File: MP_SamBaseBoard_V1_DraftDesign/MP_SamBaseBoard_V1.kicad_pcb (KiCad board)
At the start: 4 copper layers, 175 x 130.2 mm, 268 parts, among them J1 MOTOR-A_CONN, J10 P1_CONN, J11 I2C_CONN, J12 I2C_CONN, J13 SAM_SWD, J14 WS2812_EXT, J15 PWR_JACK, J16 USB_B_Micro, J17 BATT_CONN, J2 MOTOR-B_CONN, J3 Adafruit_Feather_CONN, J4 uSD_Card, J5 Conn_01x02, J6 Conn_01x02, J7 SERVO_CONN, J8 P3_CONN, J9 P2_CONN, Q1 DMP3098L, SW1 RESET, SW2 3v3_PWR_SW, SW3 SW1, SW4 SW2, U1 ESP32-WROOM-32, U10 MPU-6050, U11 IRFHM9331PbF, U12 BD5291FVE-GTR, U13 SST25VF016B-50-4C-S2AF, U2 ATSAMD51J19A-A, U3 74LVC1G125, U4 TPS62135, U5 TPS62086, U6 MAX98357AETE, U7 DRV8833RTY, U8 HDC1080, U9 MCP73871-1CC, Y1 Crystal

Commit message: update
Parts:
- added C44: 0.1uF, Capacitor_SMD:C_0603_1608Metric, F.Cu at (222.5, 179.0)
- added G***: LOGO, GiraffeTech-Utility:MakerPlayground_logo_4x4mm, F.Cu at (199.2, 182.5)
- moved R26 52.7 mm to (207.5, 179.0), turned to 270 degrees
- moved C33 52.1 mm to (210.5, 179.0), turned to 270 degrees
- moved U12 50.8 mm to (212.8, 179.0), turned to 90 degrees
- moved R27 50.3 mm to (209.0, 179.0), turned to 90 degrees
- moved R28 47.5 mm to (216.5, 179.0), turned to 270 degrees
- moved R29 44.3 mm to (215.0, 179.0), turned to 90 degrees
- moved C19 42.3 mm to (212.8, 176.5), turned to 180 degrees
- moved MK1 38.1 mm to (220.2, 179.0)
- moved C32 37.0 mm to (218.0, 179.0), turned to 90 degrees
- moved C30 34.1 mm to (228.0, 176.5)
- moved C22 21.4 mm to (264.2, 175.5)
- moved U8 21.4 mm to (267.0, 175.5)
- moved C28 18.5 mm to (240.5, 178.2), turned to 0 degrees
- moved R22 11.6 mm to (240.5, 179.8), turned to 180 degrees
- moved C29 10.1 mm to (246.8, 173.0), turned to 180 degrees
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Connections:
- U6 pad 16: D1_TxD0 -> GND
- U6 pad 17: GND -> (no net)
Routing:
- net +3V3: track 383.1 -> 427.8 mm
- net I2C_SDA: track 60.7 -> 82.1 mm
- net I2C_SCL: track 61.3 -> 81.1 mm
- net Adf_A5: track 13.2 -> 20.2 mm
- net Adf_D6: track 29.1 -> 23.1 mm
- net Net-(C33-Pad2): track 0.00 -> 5.44 mm
- net Net-(R28-Pad1): track 0.00 -> 4.88 mm
- net Net-(R22-Pad2): track 0.00 -> 4.22 mm
- net Net-(C28-Pad1): track 0.00 -> 3.39 mm
- net Net-(J6-Pad2): track 9.20 -> 11.8 mm
- net GND: track 42.9 -> 45.3 mm, vias 142 -> 174
- net Net-(C32-Pad2): track 0.00 -> 1.72 mm
- net Net-(C32-Pad1): track 0.00 -> 1.52 mm
- net Net-(C30-Pad1): track 0.00 -> 1.15 mm
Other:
- board text added: "MIC"

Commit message: update1
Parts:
- moved REF** 23.8 mm to (220.2, 205.8)
- moved C22 21.8 mm to (242.8, 179.0), turned to 90 degrees
- moved U8 21.0 mm to (246.0, 175.5)
- moved C29 6.73 mm to (240.5, 175.5), turned to 0 degrees
- moved C30 3.58 mm to (231.5, 175.8)
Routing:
- net Adf_D4: track 53.4 -> 84.2 mm
- net I2C_SDA: track 82.1 -> 103.1 mm, vias 1 -> 2
- net I2C_SCL: track 81.1 -> 96.1 mm, vias 1 -> 2
- net +3V3: track 427.8 -> 435.9 mm, vias 9 -> 12
- net SWDIO: track 16.4 -> 12.9 mm
- net GND: track 45.3 -> 48.1 mm, vias 174 -> 178
- net Adf_D13: track 35.8 -> 38.2 mm
- net SPI_MISO: track 81.6 -> 83.7 mm
- net SPI_SCK: track 85.6 -> 87.5 mm
- net SPI_MOSI: track 72.8 -> 74.7 mm
- net Adf_A4: track 41.4 -> 42.8 mm
- net SWCLK: track 12.7 -> 13.7 mm, vias 2 -> 1
- net Net-(C30-Pad1): track 1.15 -> 1.90 mm
- net SWO: track 14.5 -> 13.8 mm
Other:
- board text added: "6V-15V"
- board text added: "OFF"
- board text added: "TEMP&HUMID"

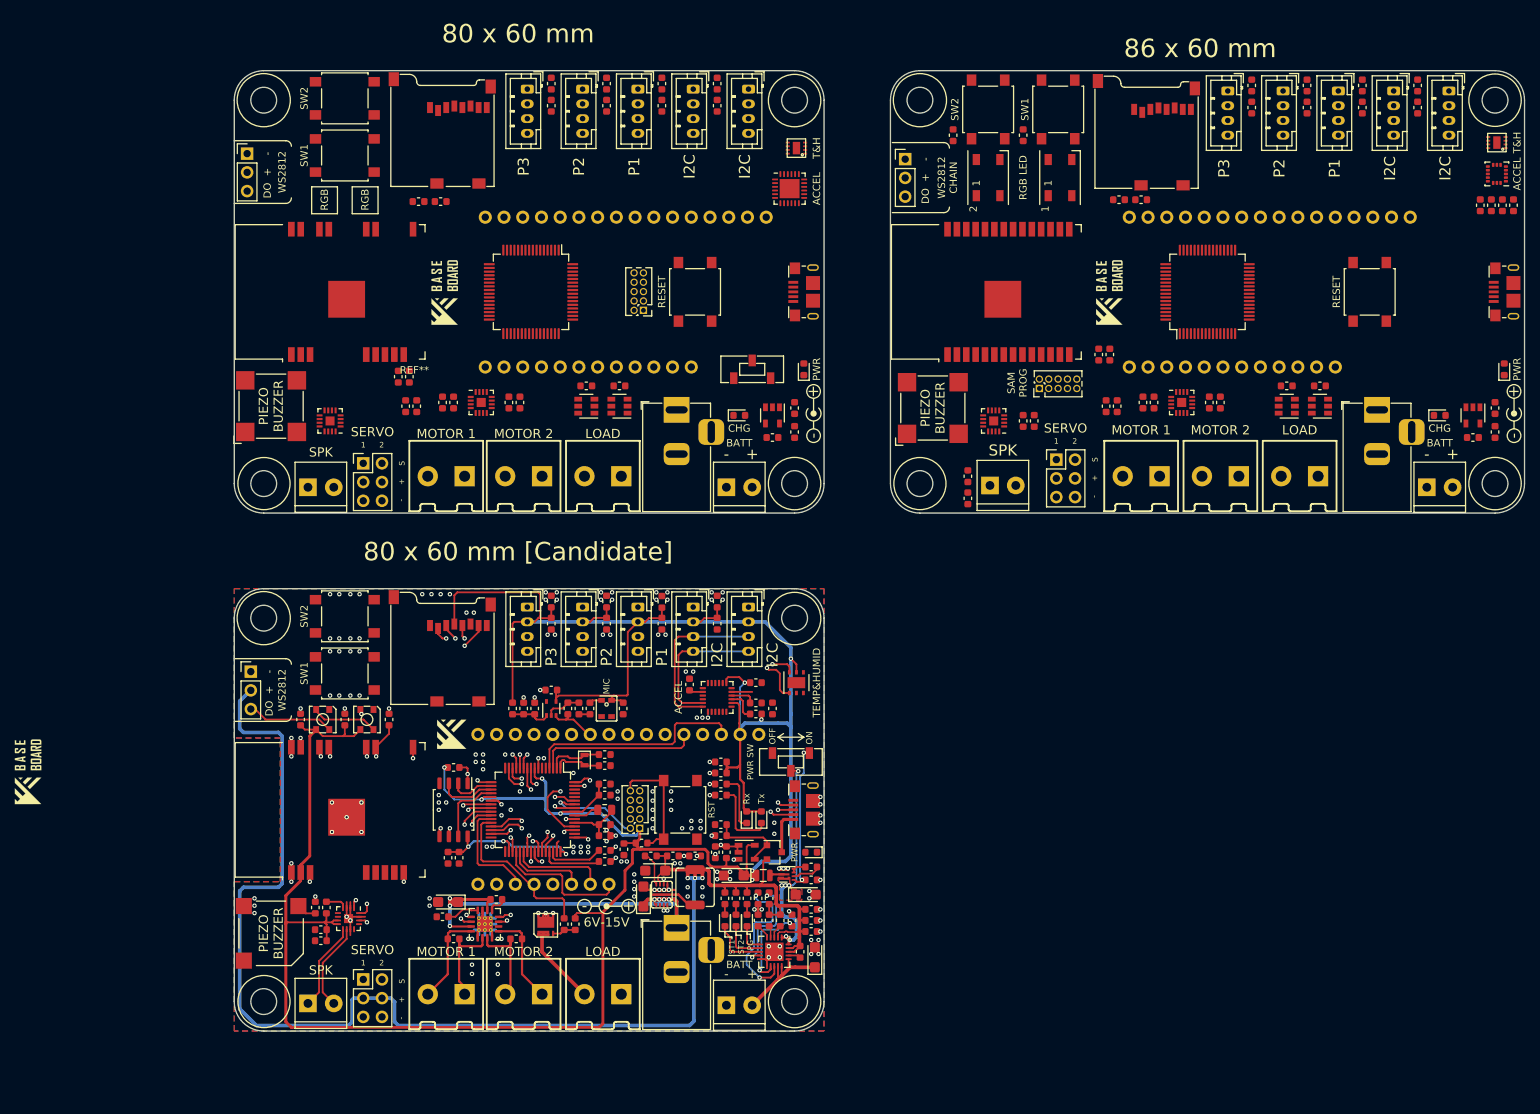
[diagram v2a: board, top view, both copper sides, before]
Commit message: Footprint replacement pending
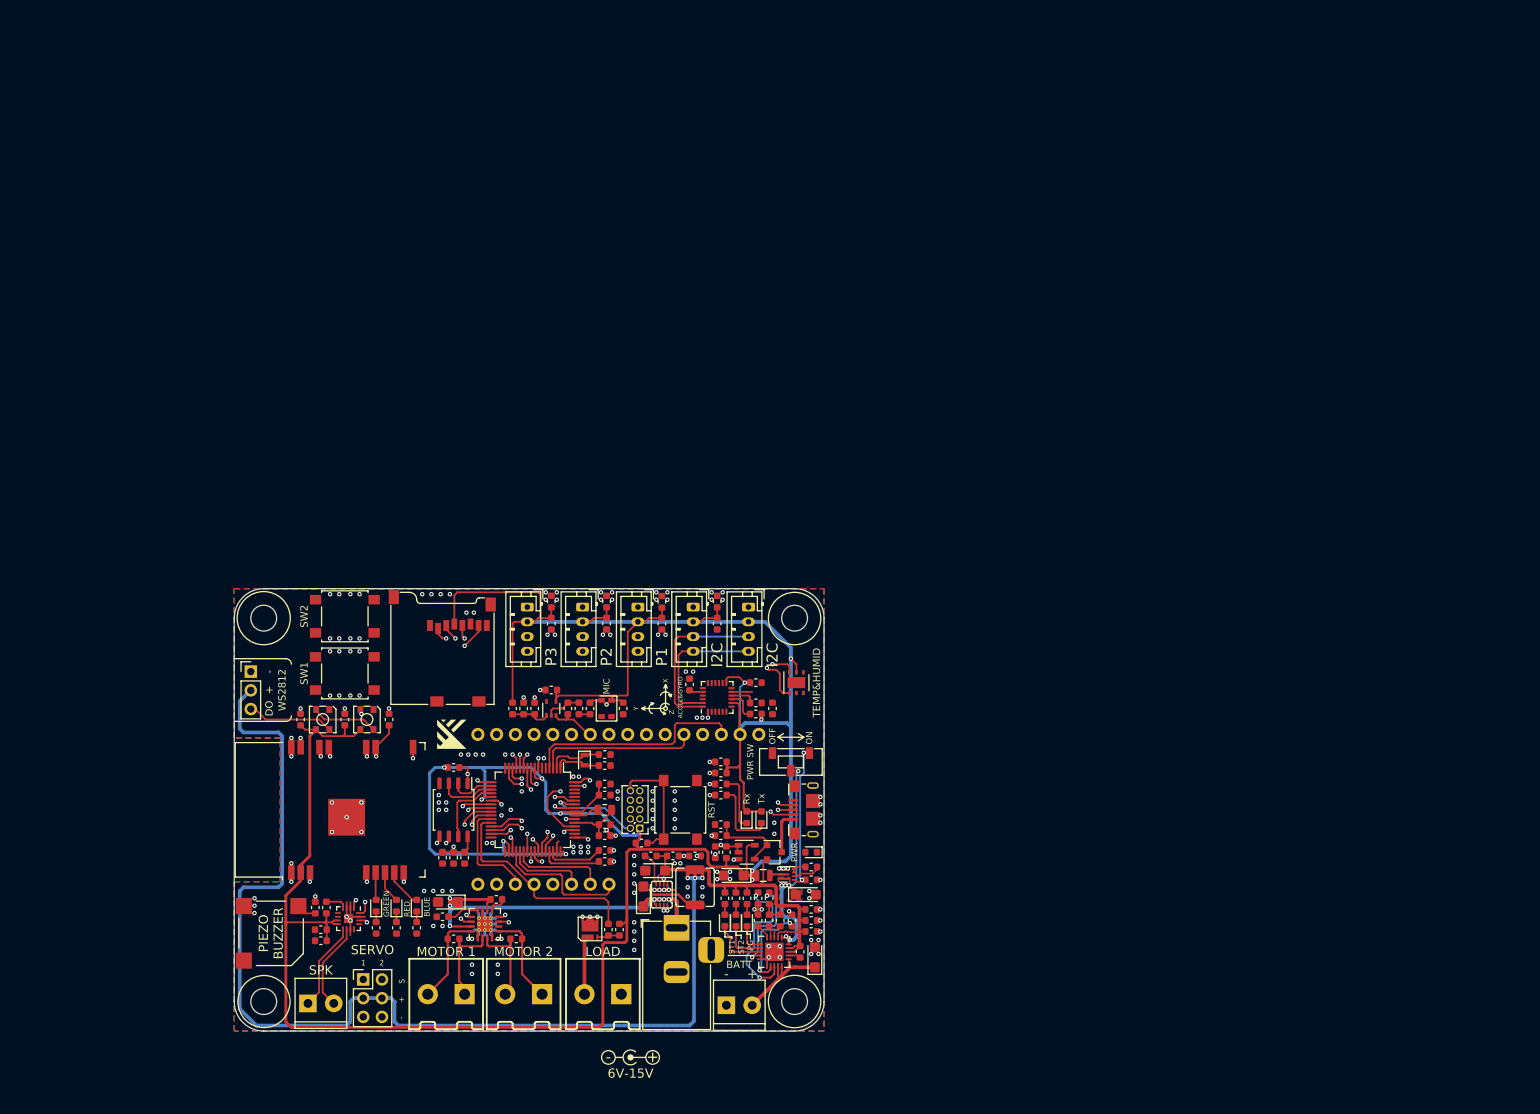
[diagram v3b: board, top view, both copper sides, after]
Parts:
- removed the G*** at (141.8, 187.5)
- removed the G*** at (198.2, 122.5)
- removed the G*** at (288.4, 122.5)
- removed MS2 (x2): FEATHERWING_NODIM, GiraffeTech-Connector:Adafruit-Feather_WoMountPoint
- removed the REF** at (220.2, 205.8)
- removed the REF** at (184.8, 104.0)
- removed the REF** at (333.2, 149.0)
- removed the REF** at (292.8, 147.5)
- removed the REF** at (342.0, 133.0)
- removed the REF** at (340.8, 148.5)
- removed the REF** at (317.0, 138.0)
- removed the REF** at (303.5, 137.5)
- removed the REF** at (302.0, 137.5)
- removed the REF** at (337.8, 139.2)
- removed the REF** at (312.5, 138.0)
- removed the REF** at (274.0, 148.8)
- removed the REF** at (245.8, 141.5)
- removed the REF** at (303.5, 147.5)
- removed the REF** at (299.5, 97.8)
- removed the REF** at (334.5, 95.2)
- removed the REF** at (262.8, 148.5)
- removed the REF** at (327.0, 95.2)
- removed the REF** at (343.2, 122.5)
- removed the REF** at (293.0, 137.5)
- removed the REF** at (294.5, 137.5)
- removed the REF** at (340.8, 138.2)
- removed the REF** at (341.0, 106.5)
- removed the REF** at (198.0, 137.5)
- removed the REF** at (319.5, 95.2)
- removed the REF** at (288.5, 131.0)
- removed the REF** at (337.8, 142.2)
- removed the REF** at (333.2, 139.2)
- removed the REF** at (281.5, 97.8)
- removed the REF** at (278.9, 135.6)
- removed the REF** at (304.5, 95.2)
- removed the REF** at (281.8, 107.0)
- removed the REF** at (262.8, 96.5)
- removed the REF** at (274.8, 122.5)
- removed the REF** at (248.2, 139.0)
- removed the REF** at (312.5, 135.2)
- removed the REF** at (301.8, 122.5)
- removed the REF** at (314.2, 147.5)
- removed the REF** at (340.8, 96.5)
- removed the REF** at (317.0, 135.2)
- removed the REF** at (267.2, 101.2)
- removed the REF** at (264.5, 138.2)
- removed the REF** at (220.2, 94.2)
- removed the REF** at (204.0, 97.5)
- removed the REF** at (235.2, 94.2)
- removed the REF** at (203.2, 137.5)
- removed the REF** at (174.8, 138.0)
- removed the REF** at (198.5, 147.5)
- removed the REF** at (193.0, 138.0)
- removed the REF** at (238.2, 149.0)
- removed the REF** at (208.5, 137.5)
- removed the REF** at (182.8, 140.0)
- removed the REF** at (173.8, 148.5)
- removed the REF** at (245.8, 148.5)
- removed the REF** at (222.0, 138.0)
- removed the REF** at (225.2, 125.0)
- removed the REF** at (239.5, 95.0)
- removed the REF** at (220.2, 97.2)
- removed the REF** at (192.0, 134.0)
- removed the REF** at (194.8, 110.2)
- removed the REF** at (187.2, 145.8)
- removed the REF** at (248.2, 122.5)
- removed the REF** at (217.5, 135.2)
- removed the REF** at (232.2, 122.5)
- removed the REF** at (235.2, 97.2)
- removed the REF** at (224.5, 95.0)
- removed the REF** at (199.5, 137.5)
- removed the REF** at (222.0, 135.2)
- removed the REF** at (245.8, 96.5)
- removed the REF** at (219.8, 147.5)
- removed the REF** at (210.0, 122.5)
- removed the REF** at (197.8, 110.2)
- removed the REF** at (212.8, 94.2)
- removed the REF** at (181.5, 149.0)
- removed the REF** at (229.8, 138.5)
- removed the REF** at (246.0, 103.0)
- removed the REF** at (238.2, 139.2)
- removed the REF** at (242.8, 142.2)
- removed the REF** at (245.8, 138.2)
- removed the REF** at (232.0, 95.0)
- removed the REF** at (194.5, 138.0)
- removed the REF** at (209.5, 95.0)
- removed the REF** at (227.8, 97.2)
- removed the REF** at (227.8, 94.2)
- removed the REF** at (217.0, 95.0)
- removed the REF** at (193.5, 134.0)
- removed the REF** at (247.0, 133.0)
- removed the REF** at (242.8, 139.2)
- removed the REF** at (245.1, 108.5)
- removed the REF** at (207.0, 137.5)
- removed the REF** at (209.0, 147.5)
- removed the REF** at (171.5, 103.8)
- removed the REF** at (173.8, 96.5)
- removed the REF** at (217.5, 138.0)
- removed the REF** at (212.8, 97.2)
- removed the REF** at (292.8, 110.0)
- removed the REF** at (289.8, 110.0)
- removed the REF** at (278.2, 140.0)
- removed the REF** at (276.8, 140.0)
- removed the REF** at (185.8, 122.5)
- removed the REF** at (269.2, 147.5)
- removed the REF** at (269.2, 150.5)
- removed the REF** at (338.8, 110.8)
- removed the REF** at (307.8, 97.5)
- removed the REF** at (307.8, 94.5)
- removed the REF** at (315.2, 94.5)
- removed the REF** at (315.2, 97.5)
- removed the REF** at (322.8, 94.5)
- removed the REF** at (322.8, 97.5)
- removed the REF** at (330.2, 97.5)
- removed the REF** at (240.0, 133.0)
- removed the REF** at (343.2, 110.8)
- removed the REF** at (341.8, 110.8)
- removed the REF** at (330.2, 94.5)
- removed the REF** at (340.2, 110.8)
- removed the REF** at (260.8, 104.5)
- removed the REF** at (343.2, 139.0)
- removed the REF** at (272.8, 140.0)
- removed the REF** at (281.2, 145.2)
- removed the REF** at (276.8, 101.2)
- removed the REF** at (298.2, 137.5)
- removed the REF** at (184.8, 96.2)
- removed the REF** at (324.8, 138.5)
- removed the REF** at (340.8, 141.5)
- removed the REF** at (312.0, 95.2)
- removed the REF** at (272.0, 97.8)
- removed the REF** at (323.8, 122.5)
- removed the REF** at (287.0, 131.0)
- removed the REF** at (288.0, 138.0)
- removed the REF** at (341.0, 102.2)
- removed the REF** at (272.0, 107.0)
- removed the REF** at (289.5, 138.0)
- added D10: RED, LED_SMD:LED_0603_1608Metric, F.Cu at (191.8, 205.8)
- added D11: BLUE, LED_SMD:LED_0603_1608Metric, F.Cu at (194.5, 205.8)
- added D9: GREEN, LED_SMD:LED_0603_1608Metric, F.Cu at (189.0, 205.8)
- added R36: 1K, Resistor_SMD:R_0603_1608Metric, F.Cu at (189.0, 208.8)
- added R37: 1K, Resistor_SMD:R_0603_1608Metric, F.Cu at (191.8, 208.8)
- added R38: 1K, Resistor_SMD:R_0603_1608Metric, F.Cu at (194.5, 208.8)
- added REF**: Symbol_Barrel_Polarity, Symbol:Symbol_Barrel_Polarity, F.Cu at (223.5, 226.2)
- J4: value uSD_Card -> GTK_TFMS08TK-PP-02
- moved C10 24.6 mm to (198.0, 199.2)
- moved R24 6.05 mm to (220.5, 209.0)
- moved R25 6.05 mm to (222.0, 209.0)
- moved U11 6.02 mm to (218.0, 208.9)
- moved C13 0.75 mm to (199.5, 199.2)
- moved C16 0.75 mm to (201.0, 199.2)
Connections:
- U1 pad 9: ESP_ACK -> D0_RxD0
- U6 pad 16: GND -> D1_TxD0
- U6 pad 17: (no net) -> GND
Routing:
- net D0_RxD0: track 49.7 -> 86.1 mm, vias 2 -> 3
- net +3V3: track 435.9 -> 456.4 mm
- net QSPI_SCK: track 9.11 -> 22.2 mm
- net Adf_D10: track 45.7 -> 55.3 mm
- net QSPI_IO0: track 11.7 -> 19.7 mm
- net Adf_D6: track 23.1 -> 29.7 mm
- net Adf_D11: track 51.5 -> 57.9 mm
- net BLUE_LED: track 0.00 -> 5.28 mm
- net VIN: track 85.1 -> 80.2 mm
- net RED_LED: track 0.00 -> 4.36 mm
- net Adf_D5: track 50.9 -> 46.7 mm
- net GREEN_LED: track 0.00 -> 3.74 mm
- net ~RESET: track 67.0 -> 70.1 mm
- net Net-(J6-Pad2): track 11.8 -> 9.06 mm
- net Adf_D9: track 35.6 -> 38.3 mm
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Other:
- board size 175 x 130.2 mm -> 80 x 60 mm
- board text added: "ACCEL&GYRO"
- board text added: "BLUE"
- board text added: "GREEN"
- board text added: "RED"
- board text added: "X"
- board text added: "Y"
- board text added: "Z"
- board text removed: "80 x 60 mm"
- board text removed: "80 x 60 mm [Candidate]"
- board text removed: "86 x 60 mm"
- board text removed: "ACCEL"
- board text removed: "CHG"
- board text removed: "RESET"
- board text removed: "RGB"
- board text removed: "RGB LED"
- board text removed: "SAM PROG"
- board text removed: "T&H"
- board text removed: "WS2812 CHAIN"
